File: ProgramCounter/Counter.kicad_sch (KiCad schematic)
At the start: 13 parts, among them J1 Conn_01x03, J2 Conn_01x08, J3 Conn_01x08, J4 Conn_01x02, J5 Conn_01x02, J6 Conn_01x08, J7 Conn_01x08, U1 74LS161, U2 74LS161, U3 74AHC1G04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

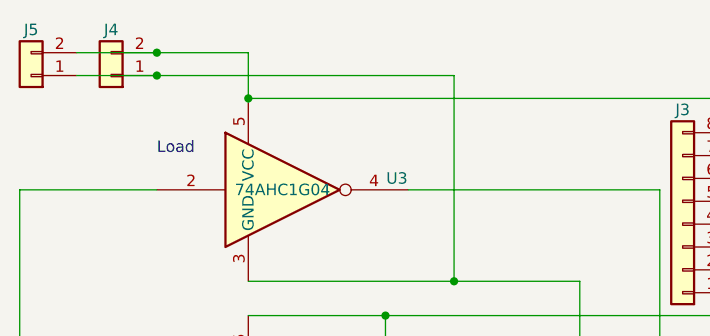
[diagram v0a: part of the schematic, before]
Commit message: Added cappacitor to all Schematic
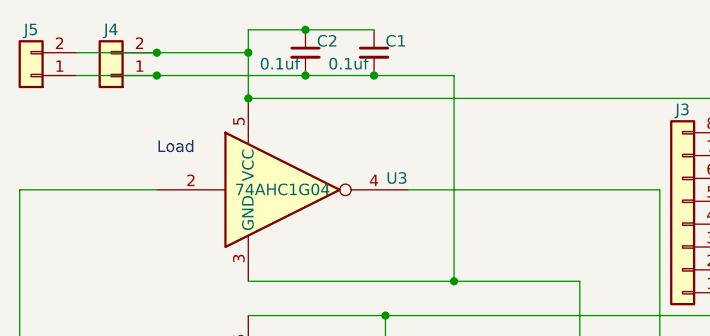
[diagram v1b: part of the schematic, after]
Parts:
- added C1, C2: 0.1uf, symbol Device:C_Small
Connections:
- net at J4.1 (Pin_1), J5.1 (Pin_1), U1.8 (GND)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: now also C1.2, C2.2
- net at J4.2 (Pin_2), J5.2 (Pin_2), U1.16 (VCC)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: now also C1.1, C2.1
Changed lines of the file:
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@@
   (junction (at 59.69 106.68) (diameter 0) (color 0 0 0 0)
   )
+  (junction (at 55.88 22.86) (diameter 0) (color 0 0 0 0)
+  )
   (junction (at 109.22 39.37) (diameter 0) (color 0 0 0 0)
   )
@@
   (junction (at 78.74 69.85) (diameter 0) (color 0 0 0 0)
   )
+  (junction (at 41.91 20.32) (diameter 0) (color 0 0 0 0)
+  )
   (junction (at 144.78 31.75) (diameter 0) (color 0 0 0 0)
   )
@@
   (junction (at 104.14 44.45) (diameter 0) (color 0 0 0 0)
   )
+  (junction (at 48.26 22.86) (diameter 0) (color 0 0 0 0)
+  )
   (junction (at 104.14 34.29) (diameter 0) (color 0 0 0 0)
   )
@@
   )
   (junction (at 41.91 25.4) (diameter 0) (color 0 0 0 0)
+  )
+  (junction (at 48.26 17.78) (diameter 0) (color 0 0 0 0)
   )
   (junction (at 102.87 46.99) (diameter 0) (color 0 0 0 0)
@@
     (stroke (width 0) (type default))
   )
+  (wire (pts (xy 48.26 22.86) (xy 55.88 22.86))
+    (stroke (width 0) (type default))
+  )
   (wire (pts (xy 128.27 83.82) (xy 129.54 83.82))
     (stroke (width 0) (type default))
@@
     (stroke (width 0) (type default))
   )
-  (wire (pts (xy 31.75 22.86) (xy 64.77 22.86))
+  (wire (pts (xy 31.75 22.86) (xy 48.26 22.86))
     (stroke (width 0) (type default))
   )
@@
     (stroke (width 0) (type default))
   )
+  (wire (pts (xy 55.88 17.78) (xy 48.26 17.78))
+    (stroke (width 0) (type default))
+  )
   (wire (pts (xy 154.94 101.6) (xy 153.67 101.6))
     (stroke (width 0) (type default))
@@
     (stroke (width 0) (type default))
   )
+  (wire (pts (xy 48.26 17.78) (xy 41.91 17.78))
+    (stroke (width 0) (type default))
+  )
+  (wire (pts (xy 41.91 17.78) (xy 41.91 20.32))
+    (stroke (width 0) (type default))
+  )
   (wire (pts (xy 115.57 114.3) (xy 167.64 114.3))
     (stroke (width 0) (type default))
@@
   )
   (wire (pts (xy 22.86 20.32) (xy 31.75 20.32))
+    (stroke (width 0) (type default))
+  )
+  (wire (pts (xy 55.88 22.86) (xy 64.77 22.86))
     (stroke (width 0) (type default))
   )
@@
         )
       )
+    )
+  )
+  (symbol (lib_id "Device:C_Small") (at 48.26 20.32 0) (unit 1)
+    (in_bom yes) (on_board yes) (dnp no)
+    (property "Reference" "C2" (at 49.53 19.05 0)
+      (effects (font (size 1.27 1.27)) (justify left))
+    )
+    (property "Value" "0.1uf" (at 43.18 21.59 0)
+      (effects (font (size 1.27 1.27)) (justify left))
+    )
+    (property "Footprint" "" (at 48.26 20.32 0)
+      (effects (font (size 1.27 1.27)) hide)
+    )
+    (property "Datasheet" "~" (at 48.26 20.32 0)
+      (effects (font (size 1.27 1.27)) hide)
+    )
+    (pin "1")
+    (pin "2")
+    (instances
+      (project "Counter"
+        (path "/844b9788-507c-4ea1-823f-83f0241639b6"
+          (reference "C2") (unit 1)
+        )
+      )
+    )
+  )
+  (symbol (lib_id "Device:C_Small") (at 55.88 20.32 0) (unit 1)
+    (in_bom yes) (on_board yes) (dnp no)
+    (property "Reference" "C1" (at 57.15 19.05 0)
+      (effects (font (size 1.27 1.27)) (justify left))
+    )
+    (property "Value" "0.1uf" (at 50.8 21.59 0)
+      (effects (font (size 1.27 1.27)) (justify left))
+    )
+    (property "Footprint" "" (at 55.88 20.32 0)
+      (effects (font (size 1.27 1.27)) hide)
+    )
+    (property "Datasheet" "~" (at 55.88 20.32 0)
+      (effects (font (size 1.27 1.27)) hide)
+    )
+    (pin "1")
+    (pin "2")
+    (instances
+      (project "Counter"
+        (path "/844b9788-507c-4ea1-823f-83f0241639b6"
+          (reference "C1") (unit 1)
+        )
+      )

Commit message: Started assigning footprint
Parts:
- C1, C2: footprint (none) -> Capacitor_SMD:C_0603_1608Metric_Pad1.08x0.95mm_HandSolder
- J1: footprint (none) -> Connector_PinHeader_2.54mm:PinHeader_1x03_P2.54mm_Vertical
- J2, J3, J6, J7: footprint (none) -> Connector_PinHeader_2.54mm:PinHeader_1x08_P2.54mm_Vertical
- J4, J5: footprint (none) -> Connector_PinHeader_2.54mm:PinHeader_1x02_P2.54mm_Vertical
- U1, U2: footprint (none) -> Package_SO:SOIC-16_4.55x10.3mm_P1.27mm
- U3, U4, U6: footprint (none) -> Package_SO:TSOP-5_1.65x3.05mm_P0.95mm
- U5: footprint (none) -> Package_SO:SOIC-14W_7.5x9mm_P1.27mm
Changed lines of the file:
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@@
       (effects (font (size 1.27 1.27)) hide)
     )
-    (property "Footprint" "" (at 99.06 39.37 0)
+    (property "Footprint" "Connector_PinHeader_2.54mm:PinHeader_1x08_P2.54mm_Vertical" (at 99.06 39.37 0)
       (effects (font (size 1.27 1.27)) hide)
     )
@@
       (effects (font (size 1.27 1.27)) hide)
     )
-    (property "Footprint" "" (at 22.86 137.16 0)
+    (property "Footprint" "Connector_PinHeader_2.54mm:PinHeader_1x08_P2.54mm_Vertical" (at 22.86 137.16 0)
       (effects (font (size 1.27 1.27)) hide)
     )
@@
       (effects (font (size 1.27 1.27)) hide)
     )
-    (property "Footprint" "" (at 37.2222 137.3473 0)
+    (property "Footprint" "Connector_PinHeader_2.54mm:PinHeader_1x08_P2.54mm_Vertical" (at 37.2222 137.3473 0)
       (effects (font (size 1.27 1.27)) hide)
     )
@@
       (effects (font (size 1.27 1.27)) hide)
     )
-    (property "Footprint" "" (at 26.67 22.86 0)
+    (property "Footprint" "Connector_PinHeader_2.54mm:PinHeader_1x02_P2.54mm_Vertical" (at 26.67 22.86 0)
       (effects (font (size 1.27 1.27)) hide)
     )
@@
       (effects (font (size 1.27 1.27)) (justify left))
     )
-    (property "Footprint" "" (at 115.57 93.98 0)
+    (property "Footprint" "Package_SO:SOIC-16_4.55x10.3mm_P1.27mm" (at 115.57 93.98 0)
       (effects (font (size 1.27 1.27)) hide)
     )
@@
       (effects (font (size 1.27 1.27)) (justify left))
     )
-    (property "Footprint" "" (at 167.64 93.98 0)
+    (property "Footprint" "Package_SO:SOIC-16_4.55x10.3mm_P1.27mm" (at 167.64 93.98 0)
       (effects (font (size 1.27 1.27)) hide)
     )
@@
       (effects (font (size 1.27 1.27)) (justify left))
     )
-    (property "Footprint" "" (at 172.72 41.91 0)
+    (property "Footprint" "Package_SO:SOIC-14W_7.5x9mm_P1.27mm" (at 172.72 41.91 0)
       (effects (font (size 1.27 1.27)) hide)
     )
@@
       (effects (font (size 1.27 1.27)) hide)
     )
-    (property "Footprint" "" (at 85.09 99.06 0)
+    (property "Footprint" "Connector_PinHeader_2.54mm:PinHeader_1x03_P2.54mm_Vertical" (at 85.09 99.06 0)
       (effects (font (size 1.27 1.27)) hide)
     )
@@
       (effects (font (size 1.27 1.27)) hide)
     )
-    (property "Footprint" "" (at 90.17 39.37 0)
+    (property "Footprint" "Connector_PinHeader_2.54mm:PinHeader_1x08_P2.54mm_Vertical" (at 90.17 39.37 0)
       (effects (font (size 1.27 1.27)) hide)
     )
@@
       (effects (font (size 1.27 1.27)) (justify left))
     )
-    (property "Footprint" "" (at 48.26 20.32 0)
+    (property "Footprint" "Capacitor_SMD:C_0603_1608Metric_Pad1.08x0.95mm_HandSolder" (at 48.26 20.32 0)
       (effects (font (size 1.27 1.27)) hide)
     )
@@
       (effects (font (size 1.27 1.27)) (justify left))
     )
-    (property "Footprint" "" (at 55.88 20.32 0)
+    (property "Footprint" "Capacitor_SMD:C_0603_1608Metric_Pad1.08x0.95mm_HandSolder" (at 55.88 20.32 0)
       (effects (font (size 1.27 1.27)) hide)
     )
@@
       (effects (font (size 1.27 1.27)))
     )
-    (property "Footprint" "" (at 41.91 82.55 0)
+    (property "Footprint" "Package_SO:TSOP-5_1.65x3.05mm_P0.95mm" (at 41.91 82.55 0)
       (effects (font (size 1.27 1.27)) hide)
     )
@@
       (effects (font (size 1.27 1.27)))
     )
-    (property "Footprint" "" (at 46.99 35.56 0)
+    (property "Footprint" "Package_SO:TSOP-5_1.65x3.05mm_P0.95mm" (at 46.99 35.56 0)
       (effects (font (size 1.27 1.27)) hide)
     )
@@
       (effects (font (size 1.27 1.27)) hide)
     )
-    (property "Footprint" "" (at 17.78 22.86 0)
+    (property "Footprint" "Connector_PinHeader_2.54mm:PinHeader_1x02_P2.54mm_Vertical" (at 17.78 22.86 0)
       (effects (font (size 1.27 1.27)) hide)
     )
@@
       (effects (font (size 1.27 1.27)))
     )
-    (property "Footprint" "" (at 46.99 59.69 0)
-      (effects (font (size 1.27 1.27)) hide)
-    )
+    (property "Footprint" "Package_SO:TSOP-5_1.65x3.05mm_P0.95mm" (at 46.99 59.69 0)
+      (effects (font (size 1.27 1.27)) hide)
+    )
